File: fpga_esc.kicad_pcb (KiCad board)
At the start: 4 copper layers, 57.1 x 62.9 mm, 42 parts, among them J1 Screw_Terminal_01x03, J2 Conn_01x09_Male, J3 Screw_Terminal_01x02, Q1 IRFR3806TRPBF, Q2 IRFR3806TRPBF, Q3 IRFR3806TRPBF, Q4 IRFR3806TRPBF, Q5 IRFR3806TRPBF, Q6 IRFR3806TRPBF, U1 UCC27212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

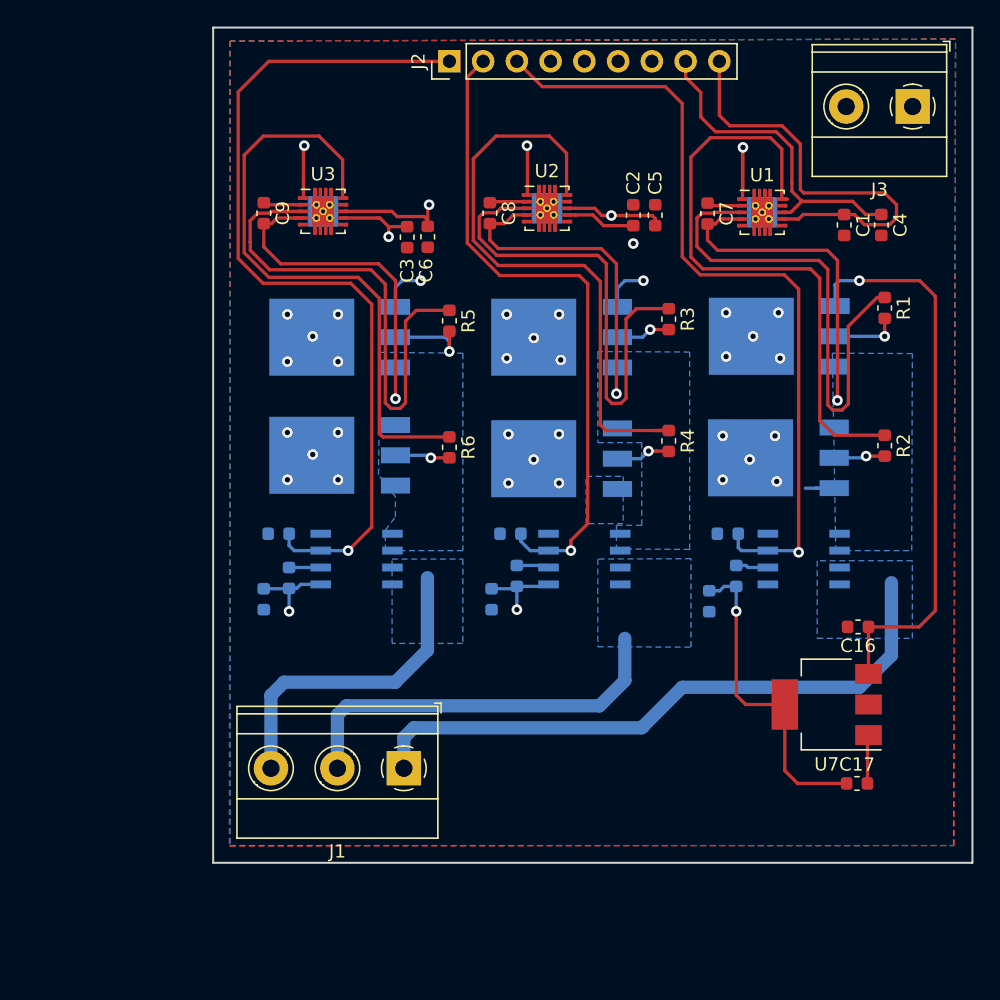
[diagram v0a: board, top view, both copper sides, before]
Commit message: Smaller form-factor
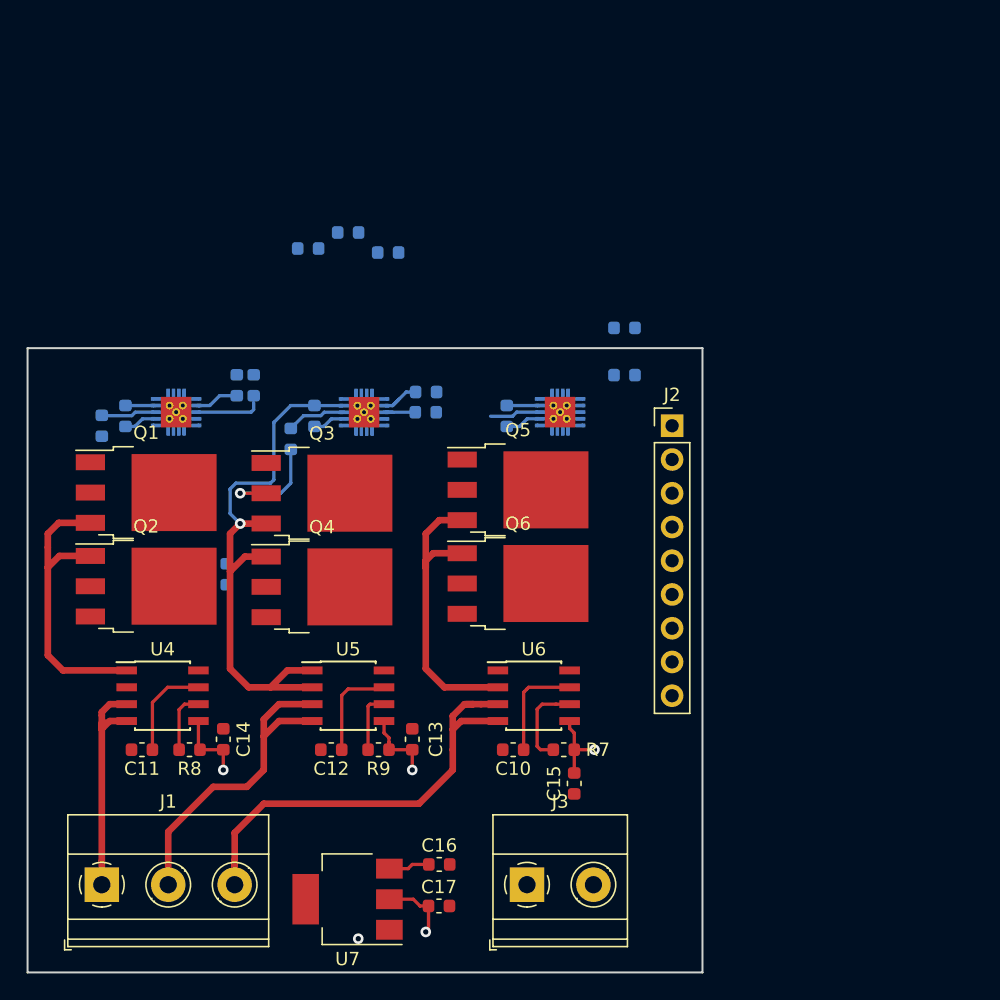
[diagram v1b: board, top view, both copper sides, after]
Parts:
- C1, C2, C3, C4, C5, C6, C7, C8, C9, R1, R2, R3, R4, R5, R6, U1, U2, U3: moved to B.Cu
- C10, C11, C12, C13, C14, C15, Q1, Q2, Q3, Q4, Q5, Q6, R7, R8, R9, U4, U5, U6: moved to F.Cu
- moved J3 65.4 mm to (131.6, 102.6), turned to 0 degrees
- moved R1 59.6 mm to (99.6, 68.1)
- moved R2 50.5 mm to (109.0, 79.2)
- moved U4 49.3 mm to (104.1, 88.4), turned to 0 degrees
- moved Q1 49.1 mm to (102.9, 73.1), turned to 0 degrees
- moved C4 48.8 mm to (111.0, 65.0), turned to 90 degrees
- moved Q2 48.6 mm to (102.9, 80.1), turned to 0 degrees
- moved C1 47.3 mm to (109.7, 65.0), turned to 90 degrees
- moved C11 47.0 mm to (102.6, 92.5)
- moved U1 46.6 mm to (105.2, 67.0)
- moved C7 46.4 mm to (101.3, 67.3), turned to 90 degrees
- moved R8 43.2 mm to (106.2, 92.5), turned to 180 degrees
- moved U7 38.9 mm to (118.1, 103.7)
- moved C16 36.2 mm to (125.0, 101.1), turned to 0 degrees
- moved C17 32.8 mm to (124.9, 104.2)
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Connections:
- U4 pad 5: Net-(U4-Pad5) -> +3V3
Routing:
- net V_POWER: track 64.5 -> 3.10 mm, vias 6 -> 0
- net /Control Signals (from FPGA or microcontroller)/VS_3: track 65.6 -> 7.94 mm, vias 1 -> 0
- net /Control Signals (from FPGA or microcontroller)/VS_1: track 60.6 -> 7.49 mm, vias 1 -> 0
- net Net-(R6-Pad1): track 46.1 -> 0.00 mm
- net Net-(R2-Pad1): track 45.9 -> 0.00 mm
- net Net-(R4-Pad1): track 45.6 -> 0.00 mm
- net /Control Signals (from FPGA or microcontroller)/VS_2: track 49.7 -> 7.52 mm, vias 1 -> 0
- net Net-(R5-Pad1): track 38.3 -> 3.89 mm
- net Net-(R1-Pad1): track 37.9 -> 3.72 mm
- net Net-(R3-Pad1): track 37.3 -> 4.54 mm
- net /Control Signals (from FPGA or microcontroller)/H3: track 29.2 -> 0.00 mm, vias 1 -> 0
- net /Control Signals (from FPGA or microcontroller)/H1: track 32.5 -> 3.39 mm
- net /Motor Output/output_1: track 47.0 -> 20.3 mm
- net /Motor Output/output_3: track 24.1 -> 50.3 mm
- net /Control Signals (from FPGA or microcontroller)/L3: track 23.4 -> 0.00 mm, vias 1 -> 0
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- removed copper zone on B.Cu, net /Motor Output/output_1
- removed copper zone on B.Cu, net /Motor Output/output_2
- removed copper zone on B.Cu, net /Motor Output/output_3
- removed copper zone on B.Cu, net /Three Phase Bridge/PHASE_1
- removed copper zone on B.Cu, net /Three Phase Bridge/PHASE_2
- removed copper zone on B.Cu, net /Three Phase Bridge/PHASE_3
- removed copper zone on B.Cu, net GND
- removed copper zone on F.Cu, net GND
- removed copper zone on In1.Cu, net GND
- removed copper zone on In2.Cu, net GND
- removed copper zone on In2.Cu, net V_POWER
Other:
- board size 57.1 x 62.9 mm -> 50.8 x 47 mm
